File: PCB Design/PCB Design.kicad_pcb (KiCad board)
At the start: 2 copper layers, 28.7 x 28.7 mm, 7 parts, among them SW1 SW_Push

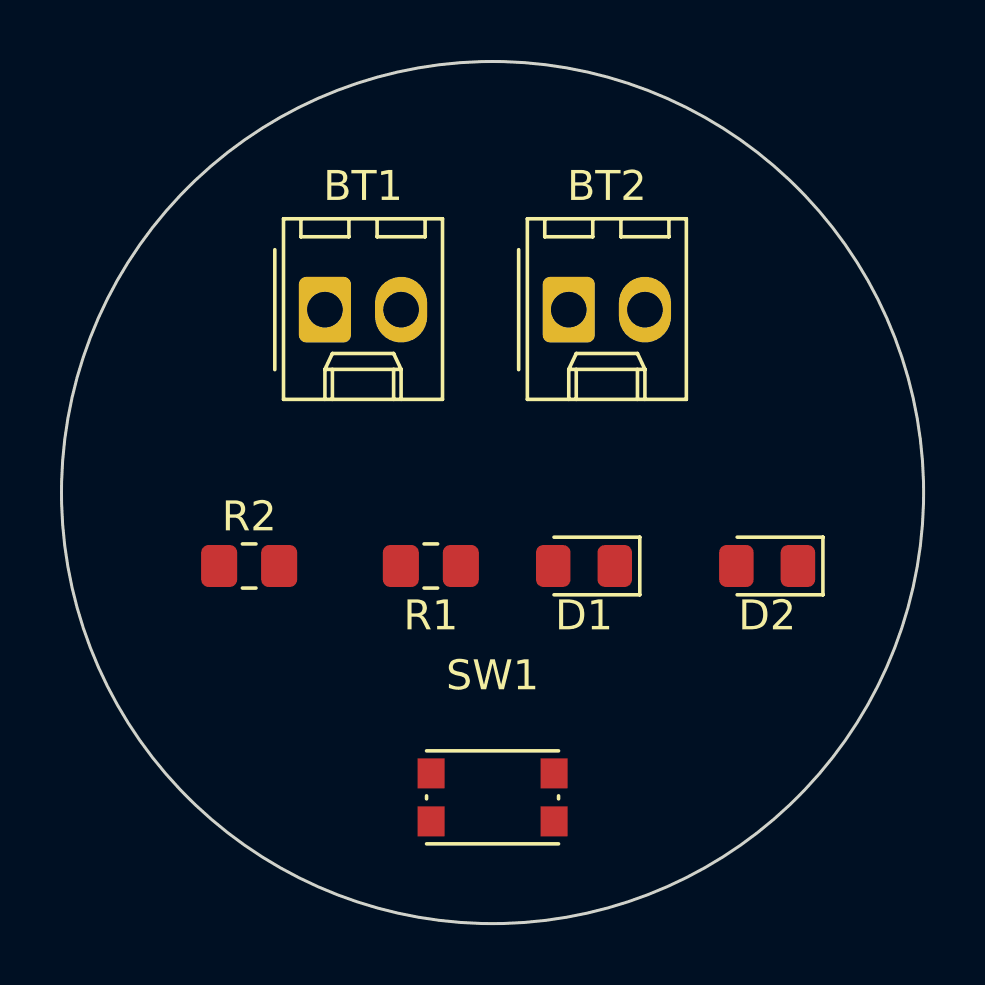
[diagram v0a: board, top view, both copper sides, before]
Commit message: SMD Routing done
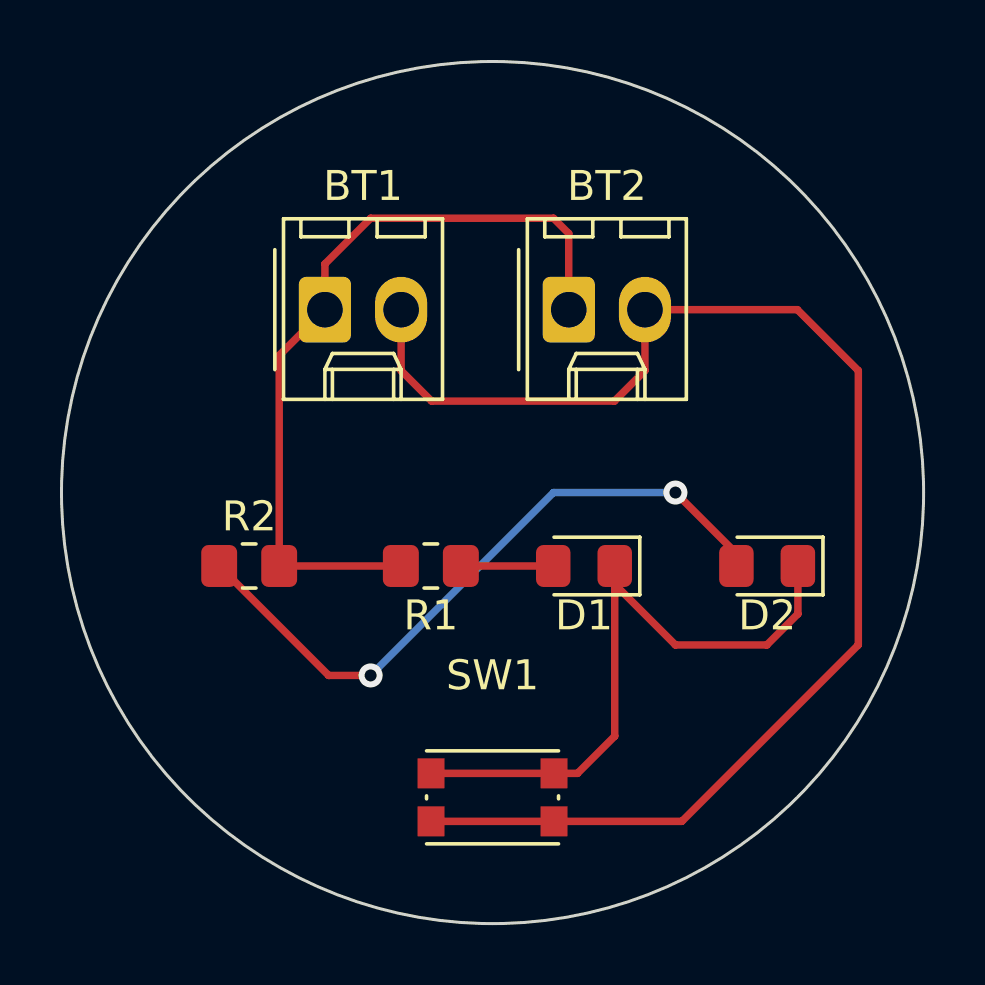
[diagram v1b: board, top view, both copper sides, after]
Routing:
- net Net-(BT1--): track 0.00 -> 46.8 mm
- net Net-(BT1-+): track 0.00 -> 26.3 mm
- net Net-(D2-A): track 0.00 -> 22.5 mm, vias 0 -> 2
- net Net-(D1-K): track 0.00 -> 21.9 mm
- net Net-(D1-A): track 0.00 -> 3.08 mm
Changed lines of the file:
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@@
   (gr_circle (center 132.08 100.584) (end 146.304 102.616)
     (stroke (width 0.1) (type default)) (fill none) (layer "Edge.Cuts"))
+  (segment (start 129.023 103.032) (end 124.968 103.032) (width 0.25) (layer "F.Cu") (net 1))
+  (segment (start 124.968 103.032) (end 124.968 96.012) (width 0.25) (layer "F.Cu") (net 1))
+  (segment (start 126.492 92.964) (end 126.492 94.488) (width 0.25) (layer "F.Cu") (net 1))
+  (segment (start 134.62 94.488) (end 134.62 91.948) (width 0.25) (layer "F.Cu") (net 1))
+  (segment (start 124.968 96.012) (end 126.492 94.488) (width 0.25) (layer "F.Cu") (net 1))
+  (segment (start 128.016 91.44) (end 126.492 92.964) (width 0.25) (layer "F.Cu") (net 1))
+  (segment (start 134.112 91.44) (end 128.016 91.44) (width 0.25) (layer "F.Cu") (net 1))
+  (segment (start 134.62 91.948) (end 134.112 91.44) (width 0.25) (layer "F.Cu") (net 1))
+  (segment (start 137.16 94.488) (end 142.24 94.488) (width 0.25) (layer "F.Cu") (net 2))
+  (segment (start 144.272 96.52) (end 144.272 105.664) (width 0.25) (layer "F.Cu") (net 2))
+  (segment (start 138.392 111.544) (end 144.272 105.664) (width 0.25) (layer "F.Cu") (net 2))
+  (segment (start 129.032 96.52) (end 130.048 97.536) (width 0.25) (layer "F.Cu") (net 2))
+  (segment (start 136.144 97.536) (end 137.16 96.52) (width 0.25) (layer "F.Cu") (net 2))
+  (segment (start 142.24 94.488) (end 144.272 96.52) (width 0.25) (layer "F.Cu") (net 2))
+  (segment (start 134.13 111.544) (end 130.03 111.544) (width 0.25) (layer "F.Cu") (net 2))
+  (segment (start 130.048 97.536) (end 136.144 97.536) (width 0.25) (layer "F.Cu") (net 2))
+  (segment (start 137.16 96.52) (end 137.16 94.488) (width 0.25) (layer "F.Cu") (net 2))
+  (segment (start 129.032 94.488) (end 129.032 96.52) (width 0.25) (layer "F.Cu") (net 2))
+  (segment (start 134.13 111.544) (end 138.392 111.544) (width 0.25) (layer "F.Cu") (net 2))
+  (segment (start 136.153 103.032) (end 136.153 108.703) (width 0.25) (layer "F.Cu") (net 3))
+  (segment (start 136.153 103.641) (end 136.153 103.032) (width 0.25) (layer "F.Cu") (net 3))
+  (segment (start 134.912 109.944) (end 134.13 109.944) (width 0.25) (layer "F.Cu") (net 3))
+  (segment (start 142.258 103.032) (end 142.258 104.63) (width 0.25) (layer "F.Cu") (net 3))
+  (segment (start 136.153 108.703) (end 134.912 109.944) (width 0.25) (layer "F.Cu") (net 3))
+  (segment (start 141.224 105.664) (end 138.176 105.664) (width 0.25) (layer "F.Cu") (net 3))
+  (segment (start 138.176 105.664) (end 136.153 103.641) (width 0.25) (layer "F.Cu") (net 3))
+  (segment (start 130.03 109.944) (end 134.13 109.944) (width 0.25) (layer "F.Cu") (net 3))
+  (segment (start 142.258 104.63) (end 141.224 105.664) (width 0.25) (layer "F.Cu") (net 3))
+  (segment (start 131.023 103.032) (end 134.103 103.032) (width 0.25) (layer "F.Cu") (net 4))
+  (segment (start 140.208 102.616) (end 138.176 100.584) (width 0.25) (layer "F.Cu") (net 5))
+  (segment (start 126.616 106.68) (end 128.016 106.68) (width 0.25) (layer "F.Cu") (net 5))
+  (segment (start 122.968 103.032) (end 126.616 106.68) (width 0.25) (layer "F.Cu") (net 5))
+  (segment (start 140.208 103.032) (end 140.208 102.616) (width 0.25) (layer "F.Cu") (net 5))
+  (via (at 138.176 100.584) (size 0.8) (drill 0.4) (layers "F.Cu" "B.Cu") (net 5))
+  (via (at 128.016 106.68) (size 0.8) (drill 0.4) (layers "F.Cu" "B.Cu") (net 5))
+  (segment (start 128.016 106.68) (end 134.112 100.584) (width 0.25) (layer "B.Cu") (net 5))
+  (segment (start 134.112 100.584) (end 138.176 100.584) (width 0.25) (layer "B.Cu") (net 5))
 )
